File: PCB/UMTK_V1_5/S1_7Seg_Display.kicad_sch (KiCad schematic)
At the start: 36 parts, among them Q1 MPSA06RLRP, Q2 MPSA06RLRP, Q3 MPSA06RLRP, Q4 MPSA06RLRP, Q5 MPSA06RLRP, Q6 MPSA06RLRP, Q7 MPSA06RLRP, Q8 MPSA06RLRP, U2 CD74AC541E, U3 CD74AC541E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

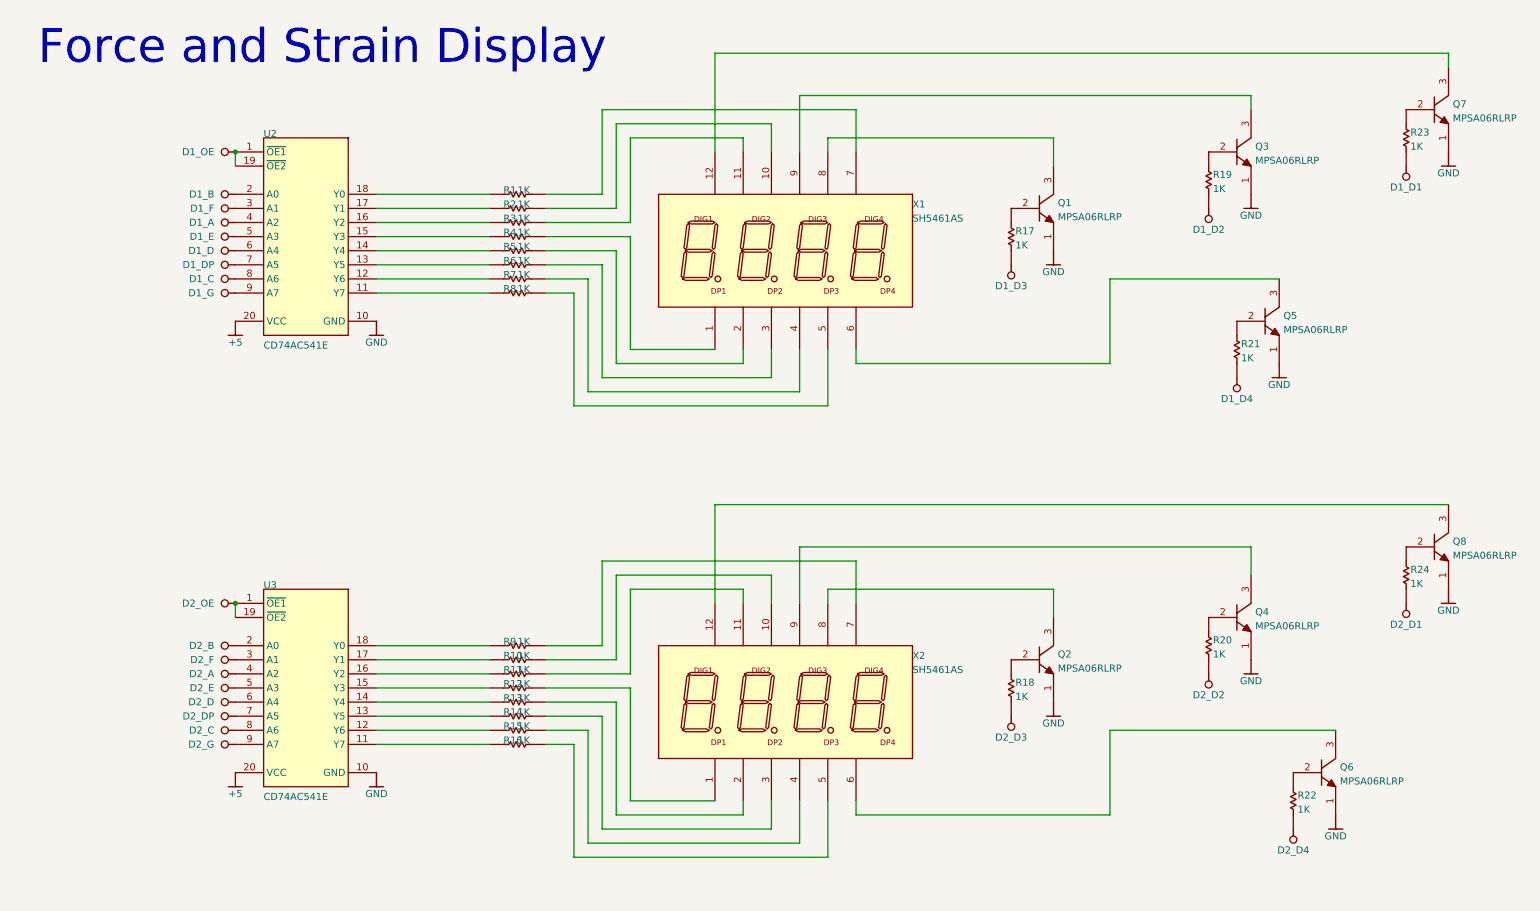
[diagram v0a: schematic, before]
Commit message: Updated Schematics
Done: 7 Seg, Power, Motor, Slide, HX711
To Do: Arduino
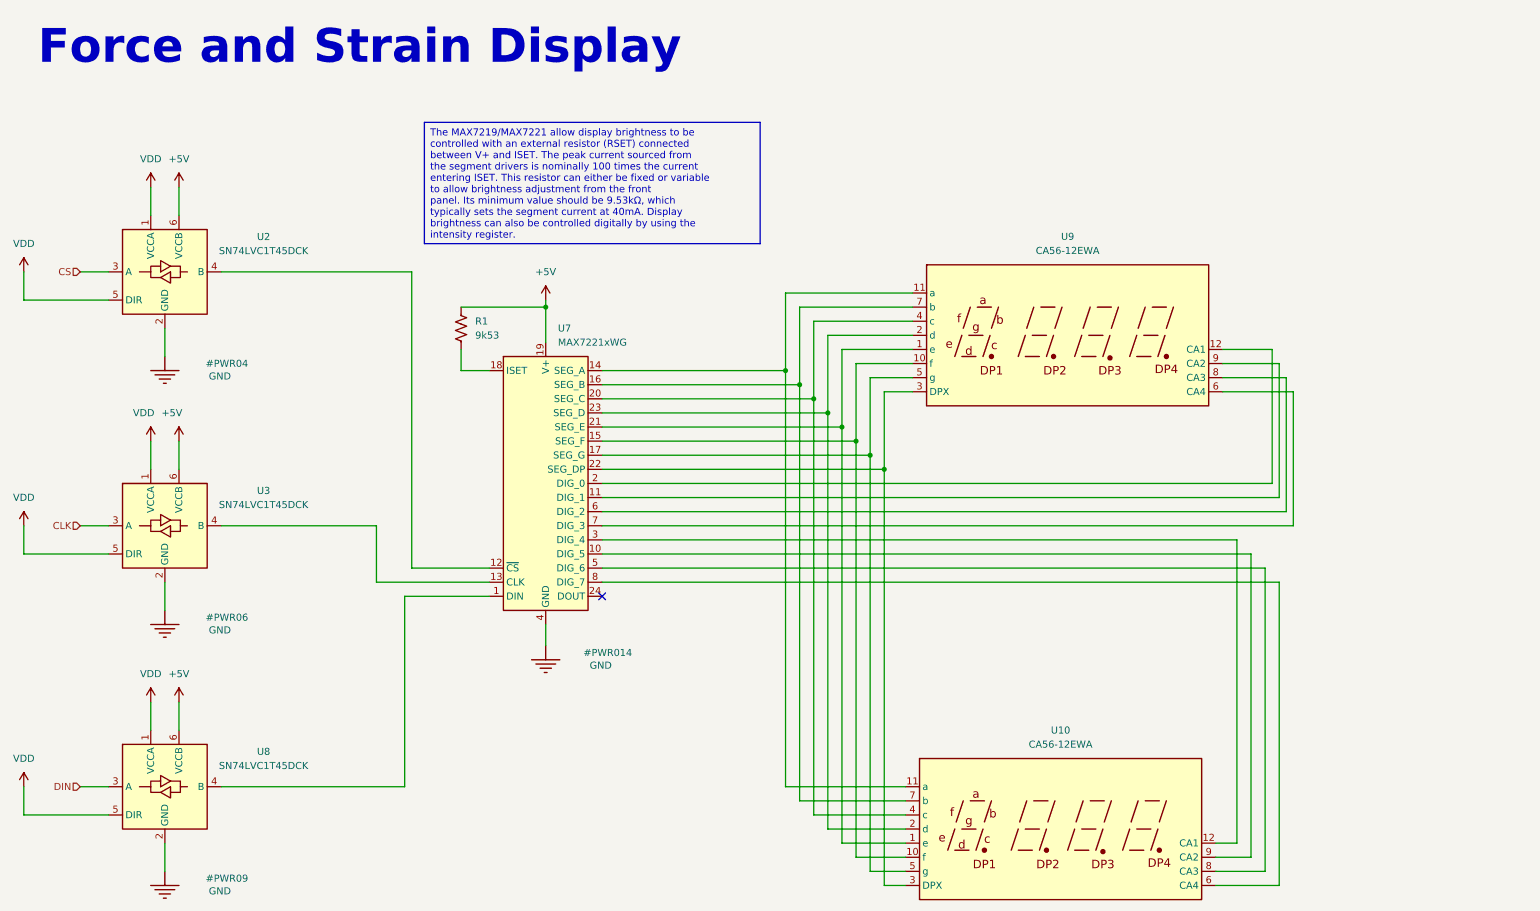
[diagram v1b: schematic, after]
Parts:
- removed Q1, Q2, Q3, Q4, Q5, Q6, Q7, Q8: MPSA06RLRP, ONSC-TO-92-3-29-11_AM_BL, symbol UMTK-altium-import:root_0_ONSC-NPN-E1B2C3-3
- removed R1, R10, R11, R12, R13, R14, R15, R16, R2, R3, R4, R5, R6, R7, R8, R9: Res1, AXIAL-0.3-3D, symbol UMTK-altium-import:root_2_Res1
- removed R17, R18, R19, R20, R21, R22, R23, R24: Res1, AXIAL-0.3-3D, symbol UMTK-altium-import:root_1_Res1
- removed U2, U3: CD74AC541E, N0020A, symbol UMTK-altium-import:root_0_TI-CD74_54XXX541-20
- removed X1, X2: SH5461AS, 4x7Seg, symbol UMTK-altium-import:root_0_4x7Seg
- added R1: 9k53, symbol Device:R_US
- added U10, U9: CA56-12EWA, Display_7Segment:CA56-12EWA, symbol Display_Character:CA56-12EWA
- added U2, U3, U8: SN74LVC1T45DCK, Package_TO_SOT_SMD:SOT-363_SC-70-6, symbol Logic_LevelTranslator:SN74LVC1T45DCK
- added U7: MAX7221xWG, Package_SO:SOIC-24W_7.5x15.4mm_P1.27mm, symbol Driver_LED:MAX7221xWG
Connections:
- net GND: now also U2.2 (GND), U3.2 (GND), U7.4 (GND), U7.9 (GND), U8.2 (GND)
- new net: U2.4 (B), U7.12 (~{CS})
- new net: R1.2, U7.18 (ISET)
- new net: U7.1 (DIN), U8.4 (B)
- new net: U10.9 (CA2), U7.10 (DIG_5)
- new net: U7.11 (DIG_1), U9.9 (CA2)
- new net: U3.4 (B), U7.13 (CLK)
- new net: U10.11 (a), U7.14 (SEG_A), U9.11 (a)
- new net: U10.10 (f), U7.15 (SEG_F), U9.10 (f)
- new net: U10.7 (b), U7.16 (SEG_B), U9.7 (b)
- new net: U10.5 (g), U7.17 (SEG_G), U9.5 (g)
- new net: U7.2 (DIG_0), U9.12 (CA1)
- new net: U10.4 (c), U7.20 (SEG_C), U9.4 (c)
- new net: U10.1 (e), U7.21 (SEG_E), U9.1 (e)
- new net: U10.3 (DPX), U7.22 (SEG_DP), U9.3 (DPX)
- new net: U10.2 (d), U7.23 (SEG_D), U9.2 (d)
- new net: U10.12 (CA1), U7.3 (DIG_4)
- new net: U10.8 (CA3), U7.5 (DIG_6)
- new net: U7.6 (DIG_2), U9.8 (CA3)
- new net: U7.7 (DIG_3), U9.6 (CA4)
- new net: U10.6 (CA4), U7.8 (DIG_7)
- new net +5V: R1.1, U2.6 (VCCB), U3.6 (VCCB), U7.19 (V+), U8.6 (VCCB)
- new net CLK: U3.3 (A)
- new net CS: U2.3 (A)
- new net DIN: U8.3 (A)
- new net VDD: U2.1 (VCCA), U2.5 (DIR), U3.1 (VCCA), U3.5 (DIR), U8.1 (VCCA), U8.5 (DIR)
- no-connect marks 0 -> 1
